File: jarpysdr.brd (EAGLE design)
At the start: 90 x 45 mm, 41 parts

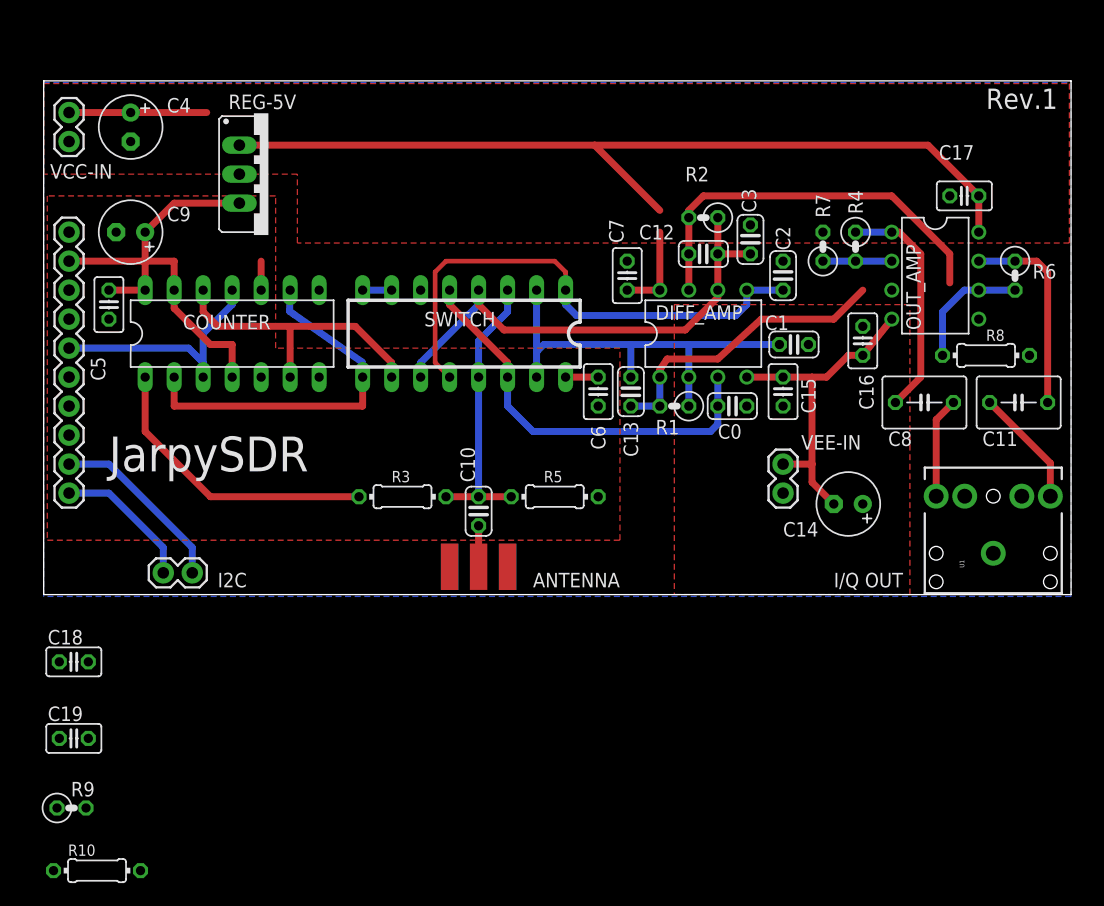
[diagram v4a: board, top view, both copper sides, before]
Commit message: Physical layout for inter-stage AC coupling.
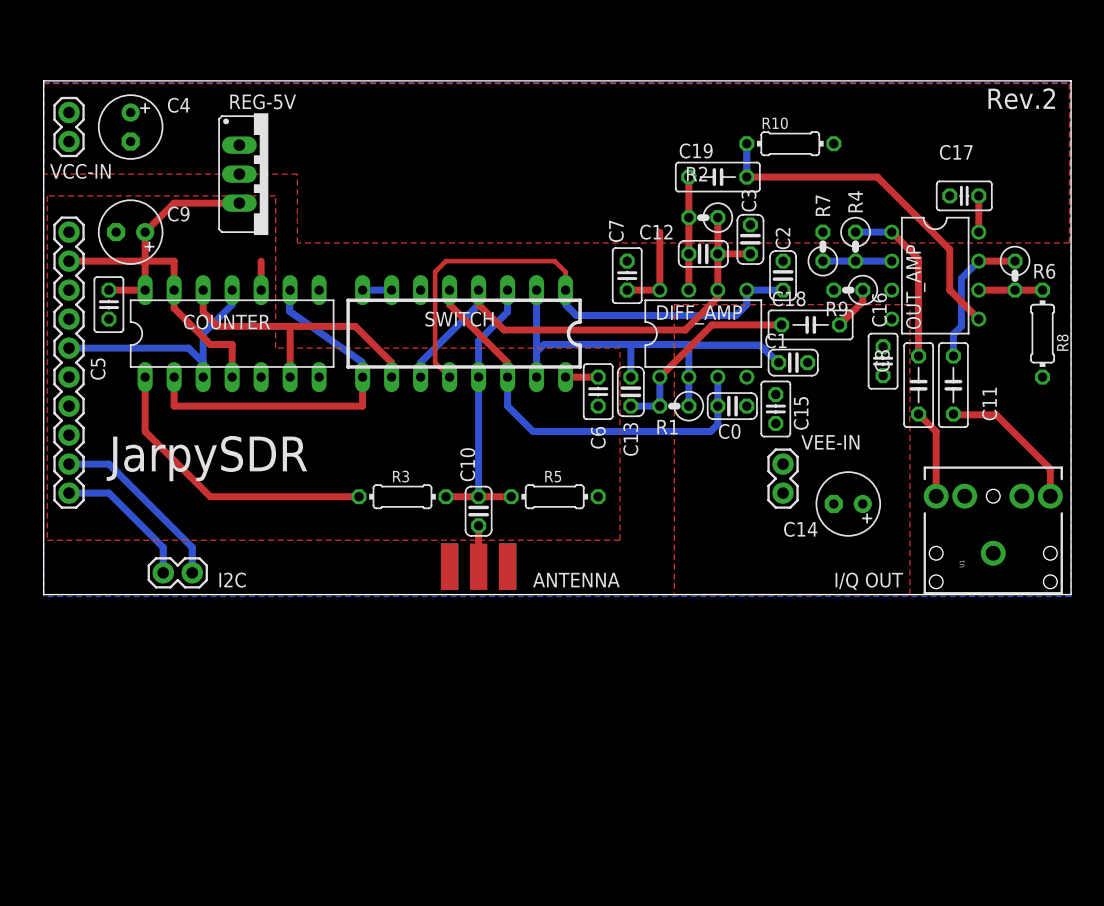
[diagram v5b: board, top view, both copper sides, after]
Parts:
- C11, C8: device resistor:C050-045X075 -> resistor:C050-025X075
- C18, C19: device resistor:C025-025X050 -> resistor:C050-025X075
- moved R10 88.0 mm to (65.4, 39.5)
- moved R9 81.8 mm to (70.5, 26.7), turned to 180 degrees
- moved C19 74.8 mm to (59.1, 36.6)
- moved C18 71.0 mm to (67.2, 23.6)
- moved C11 5.91 mm to (79.7, 18.4), turned to 270 degrees
- moved R8 5.31 mm to (87.5, 22.9), turned to 270 degrees
- moved C16 2.51 mm to (73.5, 20.4), turned to 270 degrees
- moved C15 1.65 mm to (64.1, 16.3)
- moved C8 1.61 mm to (76.6, 18.4), turned to 270 degrees
- moved C1 1.59 mm to (65.7, 20.3)
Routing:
- net +12V: track 97.9 -> 11.1 mm
- net N$19: track 0.00 -> 30.5 mm
- net -12V: track 29.5 -> 0.00 mm
- net N$10: track 35.0 -> 9.91 mm
- net N$6: track 26.4 -> 17.6 mm
- net N$13: track 17.9 -> 12.4 mm
- net N$11: track 20.4 -> 15.0 mm
- net N$15: track 10.9 -> 5.59 mm
- net N$18: track 0.00 -> 3.89 mm
- net N$8: track 10.4 -> 12.9 mm
- net N$9: track 8.83 -> 7.83 mm
- net C-180DEG: track 37.4 -> 38.1 mm
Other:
- board text added: "Rev.2"
- board text removed: "Rev.1"

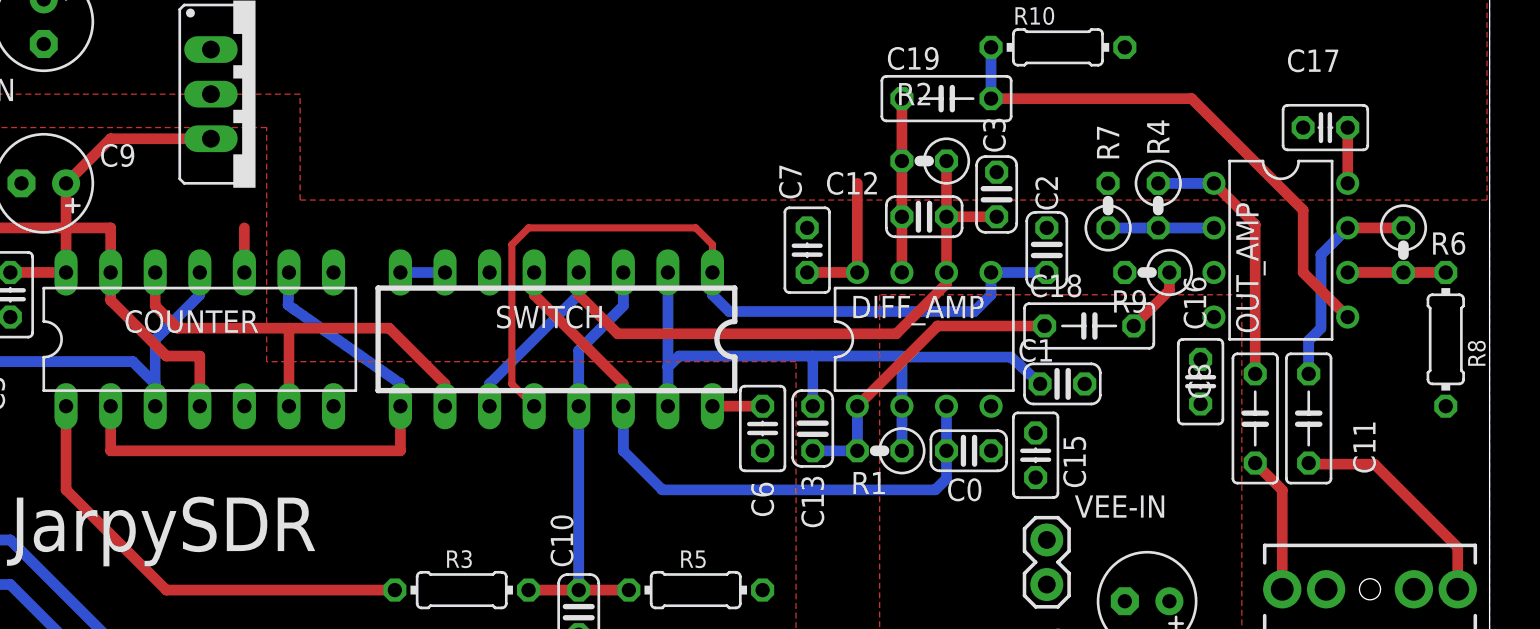
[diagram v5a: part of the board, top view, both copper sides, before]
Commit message: Put NE5532 differential amplifier on a single supply.
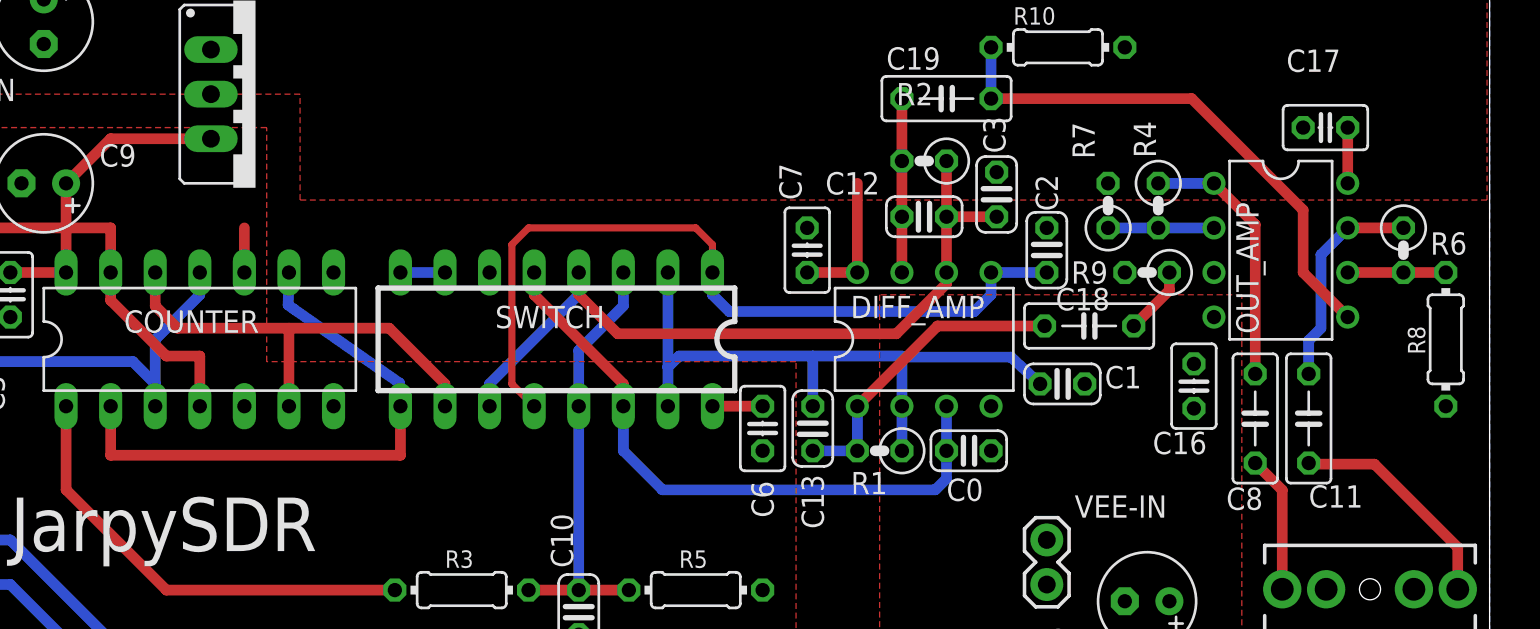
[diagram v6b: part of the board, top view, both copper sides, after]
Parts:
- removed C15: 0.1u, resistor:C025-025X050
- moved C16 0.46 mm to (73.2, 20.2)
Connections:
- net -12V: no longer C15.2, DIFF_AMP.4
- net GND: now also DIFF_AMP.4; no longer C15.1
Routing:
- net N$2: track 32.5 -> 33.0 mm
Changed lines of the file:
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@@
 </element>
 <element name="C1" library="resistor" package="C025-024X044" value="15n" x="65.659" y="20.32" smashed="yes">
-<attribute name="NAME" x="63.119" y="21.59" size="1.27" layer="25" ratio="10"/>
-<attribute name="VALUE" x="65.9765" y="21.59" size="1.27" layer="27" ratio="10"/>
+<attribute name="NAME" x="68.072" y="20.066" size="1.27" layer="25" ratio="10"/>
+<attribute name="VALUE" x="67.7545" y="18.542" size="1.27" layer="27" ratio="10"/>
 </element>
 <element name="C2" library="resistor" package="C025-024X044" value="15n" x="64.77" y="27.94" smashed="yes" rot="R90">
 <attribute name="NAME" x="65.405" y="30.1625" size="1.27" layer="25" ratio="10" rot="R90"/>
-<attribute name="VALUE" x="65.405" y="33.3375" size="1.27" layer="27" ratio="10" rot="R90"/>
+<attribute name="VALUE" x="65.405" y="32.9565" size="1.27" layer="27" ratio="10" rot="R90"/>
 </element>
 <element name="C3" library="resistor" package="C025-024X044" value="15n" x="61.9125" y="31.115" smashed="yes" rot="R90">
@@
 </element>
 <element name="C8" library="resistor" package="C050-025X075" value="0.1u" x="76.6445" y="18.3515" smashed="yes" rot="R270">
-<attribute name="NAME" x="72.8345" y="21.5265" size="1.27" layer="25" ratio="10" rot="R270"/>
-<attribute name="VALUE" x="72.8345" y="18.3515" size="1.27" layer="27" ratio="10" rot="R270"/>
+<attribute name="NAME" x="74.9935" y="13.1445" size="1.27" layer="25" ratio="10"/>
+<attribute name="VALUE" x="74.9935" y="11.6205" size="1.27" layer="27" ratio="10"/>
 </element>
 <element name="C11" library="resistor" package="C050-025X075" value="0.1u" x="79.6925" y="18.3515" smashed="yes" rot="R270">
-<attribute name="NAME" x="83.5025" y="15.1765" size="1.27" layer="25" ratio="10" rot="R90"/>
-<attribute name="VALUE" x="83.5025" y="18.9865" size="1.27" layer="27" ratio="10" rot="R90"/>
+<attribute name="NAME" x="79.6925" y="13.2715" size="1.27" layer="25" ratio="10"/>
+<attribute name="VALUE" x="79.6925" y="11.7475" size="1.27" layer="27" ratio="10"/>
 </element>
 <element name="R3" library="resistor" package="0204/7" value="2.2k" x="31.4325" y="8.5725" smashed="yes">
@@
 <attribute name="VALUE" x="64.77" y="3.4925" size="1.27" layer="27" ratio="10"/>
 </element>
-<element name="C15" library="resistor" package="C025-025X050" value="0.1u" x="64.135" y="16.256" smashed="yes" rot="R90">
-<attribute name="NAME" x="66.9925" y="14.351" size="1.27" layer="25" ratio="10" rot="R90"/>
-<attribute name="VALUE" x="68.58" y="14.351" size="1.27" layer="27" ratio="10" rot="R90"/>
-</element>
 <element name="OUT_AMP" library="linear" package="DIL08" value="TL072" x="78.105" y="27.94" smashed="yes" rot="R270">
 <attribute name="NAME" x="76.835" y="23.1775" size="1.27" layer="25" ratio="10" rot="R90"/>
@@
 </element>
 <element name="R4" library="resistor" package="0207/2V" value="120k" x="71.12" y="30.48" smashed="yes" rot="R270">
-<attribute name="NAME" x="71.755" y="33.3375" size="1.27" layer="25" ratio="10" rot="R90"/>
-<attribute name="VALUE" x="68.8975" y="36.5125" size="1.27" layer="27" ratio="10" rot="R90"/>
+<attribute name="NAME" x="70.993" y="33.2105" size="1.27" layer="25" ratio="10" rot="R90"/>
+<attribute name="VALUE" x="69.1515" y="32.5755" size="1.27" layer="27" ratio="10" rot="R90"/>
 </element>
 <element name="R6" library="resistor" package="0207/2V" value="120k" x="85.09" y="27.94" smashed="yes" rot="R270">
@@
 </element>
 <element name="R7" library="resistor" package="0207/2V" value="2.2k" x="68.2625" y="30.48" smashed="yes" rot="R90">
-<attribute name="NAME" x="68.8975" y="33.02" size="1.27" layer="25" ratio="10" rot="R90"/>
-<attribute name="VALUE" x="71.7677" y="36.4617" size="1.27" layer="27" ratio="10" rot="R90"/>
+<attribute name="NAME" x="67.5005" y="33.147" size="1.27" layer="25" ratio="10" rot="R90"/>
+<attribute name="VALUE" x="72.5297" y="33.1597" size="1.27" layer="27" ratio="10" rot="R90"/>
 </element>
 <element name="R8" library="resistor" package="0204/7" value="2.2k" x="87.503" y="22.86" smashed="yes" rot="R270">
-<attribute name="NAME" x="88.773" y="22.86" size="0.9906" layer="25" ratio="10" rot="R270"/>
+<attribute name="NAME" x="85.344" y="23.622" size="0.9906" layer="25" ratio="10" rot="R270"/>
 <attribute name="VALUE" x="87.0204" y="23.8506" size="0.9906" layer="27" ratio="10" rot="R270"/>
 </element>
-<element name="C16" library="resistor" package="C025-025X050" value="0.1u" x="73.533" y="20.447" smashed="yes" rot="R270">
-<attribute name="NAME" x="72.5805" y="26.4795" size="1.27" layer="25" ratio="10" rot="R270"/>
-<attribute name="VALUE" x="72.5805" y="17.907" size="1.27" layer="27" ratio="10" rot="R270"/>
+<element name="C16" library="resistor" package="C025-025X050" value="0.1u" x="73.152" y="20.193" smashed="yes" rot="R270">
+<attribute name="NAME" x="70.8025" y="16.3195" size="1.27" layer="25" ratio="10"/>
+<attribute name="VALUE" x="70.866" y="14.7955" size="1.27" layer="27" ratio="10"/>
 </element>
 <element name="C17" library="resistor" package="C025-025X050" value="0.1u" x="80.645" y="34.925" smashed="yes" rot="R180">
@@
 <element name="ANTENNA" library="SparkFun" package="SMA-EDGE" value="SMA_EDGE" x="40.64" y="2.4384" rot="R180"/>
 <element name="U1" library="SparkFun" package="AUDIO-JACK" value="" x="83.185" y="3.6195" rot="R90"/>
-<element name="C18" library="resistor" package="C050-025X075" value="0.1u" x="67.183" y="23.622"/>
+<element name="C18" library="resistor" package="C050-025X075" value="0.1u" x="67.183" y="23.622" smashed="yes">
+<attribute name="NAME" x="65.278" y="24.511" size="1.27" layer="25" ratio="10"/>
+<attribute name="VALUE" x="65.532" y="22.098" size="1.27" layer="27" ratio="10"/>
+</element>
 <element name="C19" library="resistor" package="C050-025X075" value="0.1u" x="59.055" y="36.576"/>
-<element name="R9" library="resistor" package="0207/2V" value="10k" x="70.485" y="26.67" rot="R180"/>
+<element name="R9" library="resistor" package="0207/2V" value="10k" x="70.485" y="26.67" smashed="yes" rot="R180">
+<attribute name="NAME" x="68.2498" y="27.305" size="1.27" layer="25" ratio="10" rot="R180"/>
+<attribute name="VALUE" x="68.5038" y="28.0162" size="1.27" layer="27" ratio="10" rot="R180"/>
+</element>
 <element name="R10" library="resistor" package="0204/7" value="10k" x="65.405" y="39.497"/>
 </elements>
@@
 <contactref element="VEE-IN" pad="2"/>
 <contactref element="C14" pad="+"/>
-<contactref element="C15" pad="1"/>
 <contactref element="R7" pad="2"/>
 <contactref element="R8" pad="2"/>
@@
 <contactref element="R10" pad="2"/>
 <contactref element="R9" pad="2"/>
+<contactref element="DIFF_AMP" pad="4"/>
+<wire x1="61.595" y1="16.51" x2="61.595" y2="19.05" width="0" layer="19" extent="1-1"/>
 <wire x1="40.64" y1="2.4384" x2="40.64" y2="2.4384" width="0" layer="19" extent="1-16"/>
 <wire x1="35.56" y1="2.4384" x2="35.56" y2="2.4384" width="0" layer="19" extent="1-16"/>
@@
 <wire x1="21.895015625" y1="24.5657375" x2="21.5425" y2="24.8125" width="0.6096" layer="16"/>
 <wire x1="21.5425" y1="24.8125" x2="21.59" y2="26.67" width="0.6096" layer="16"/>
-<wire x1="11.43" y1="19.05" x2="11.43" y2="16.51" width="0.6096" layer="1"/>
-<wire x1="11.43" y1="16.51" x2="27.94" y2="16.51" width="0.6096" layer="1"/>
-<wire x1="27.94" y1="16.51" x2="27.94" y2="19.05" width="0.6096" layer="1"/>
+<wire x1="11.43" y1="19.05" x2="11.43" y2="16.256" width="0.6096" layer="1"/>
+<wire x1="11.43" y1="16.256" x2="27.94" y2="16.256" width="0.6096" layer="1"/>
+<wire x1="27.94" y1="16.256" x2="27.94" y2="19.05" width="0.6096" layer="1"/>
 </signal>
 <signal name="N$5">
@@
 </signal>
 <signal name="-12V">
-<contactref element="DIFF_AMP" pad="4"/>
 <contactref element="VEE-IN" pad="1"/>
 <contactref element="C14" pad="-"/>
 <contactref element="OUT_AMP" pad="4"/>
-<contactref element="C15" pad="2"/>
 <contactref element="C16" pad="1"/>
 <polygon width="0.6096" layer="1">
